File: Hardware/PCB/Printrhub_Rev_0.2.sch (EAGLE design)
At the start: 67 parts, among them J1 DM3D-SF, SW1 SPST_TACT-KMR2, SW2 SPST_TACT-KMR2, U1 MK20DX256VLH7, U2 AP1117E, U3 MAX308-SOT23, Y2 16Mhz/8pF

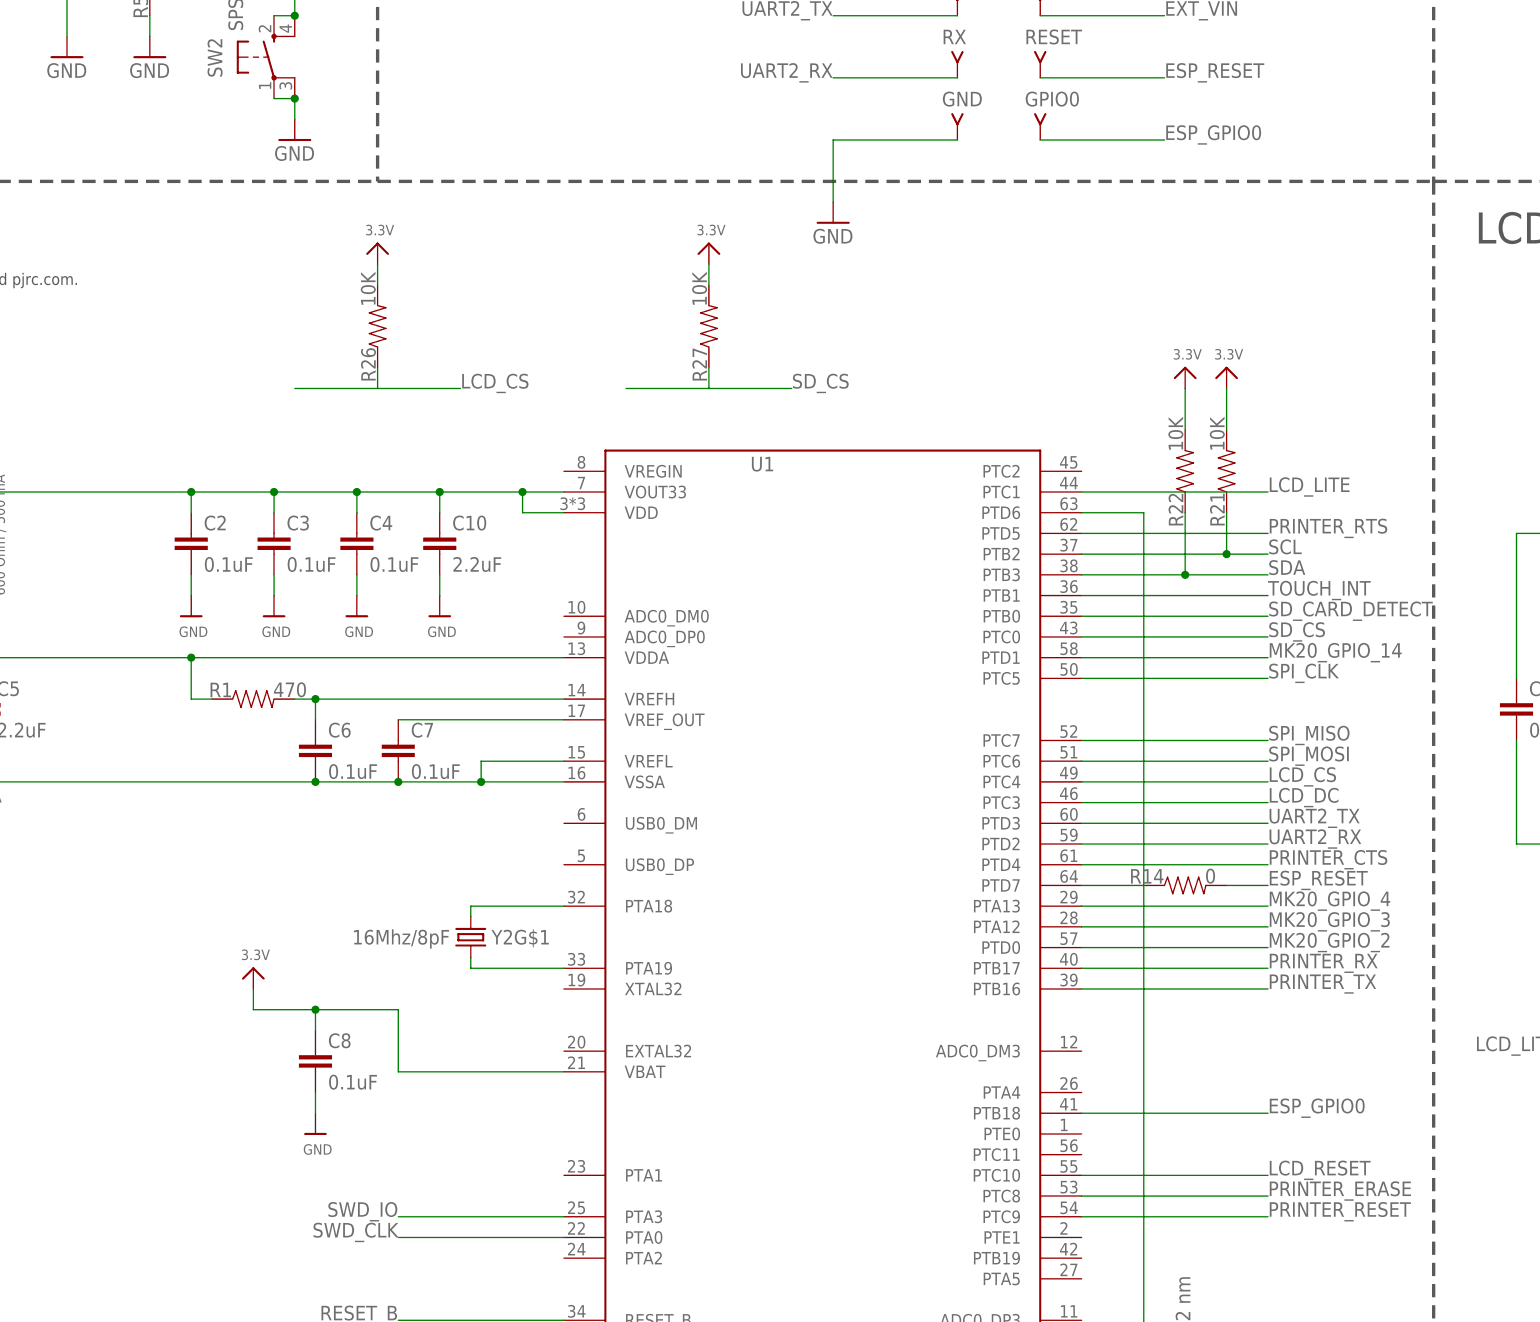
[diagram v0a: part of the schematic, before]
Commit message: Fixed a small bug in Rev 0.2 of the Printrhub PCB
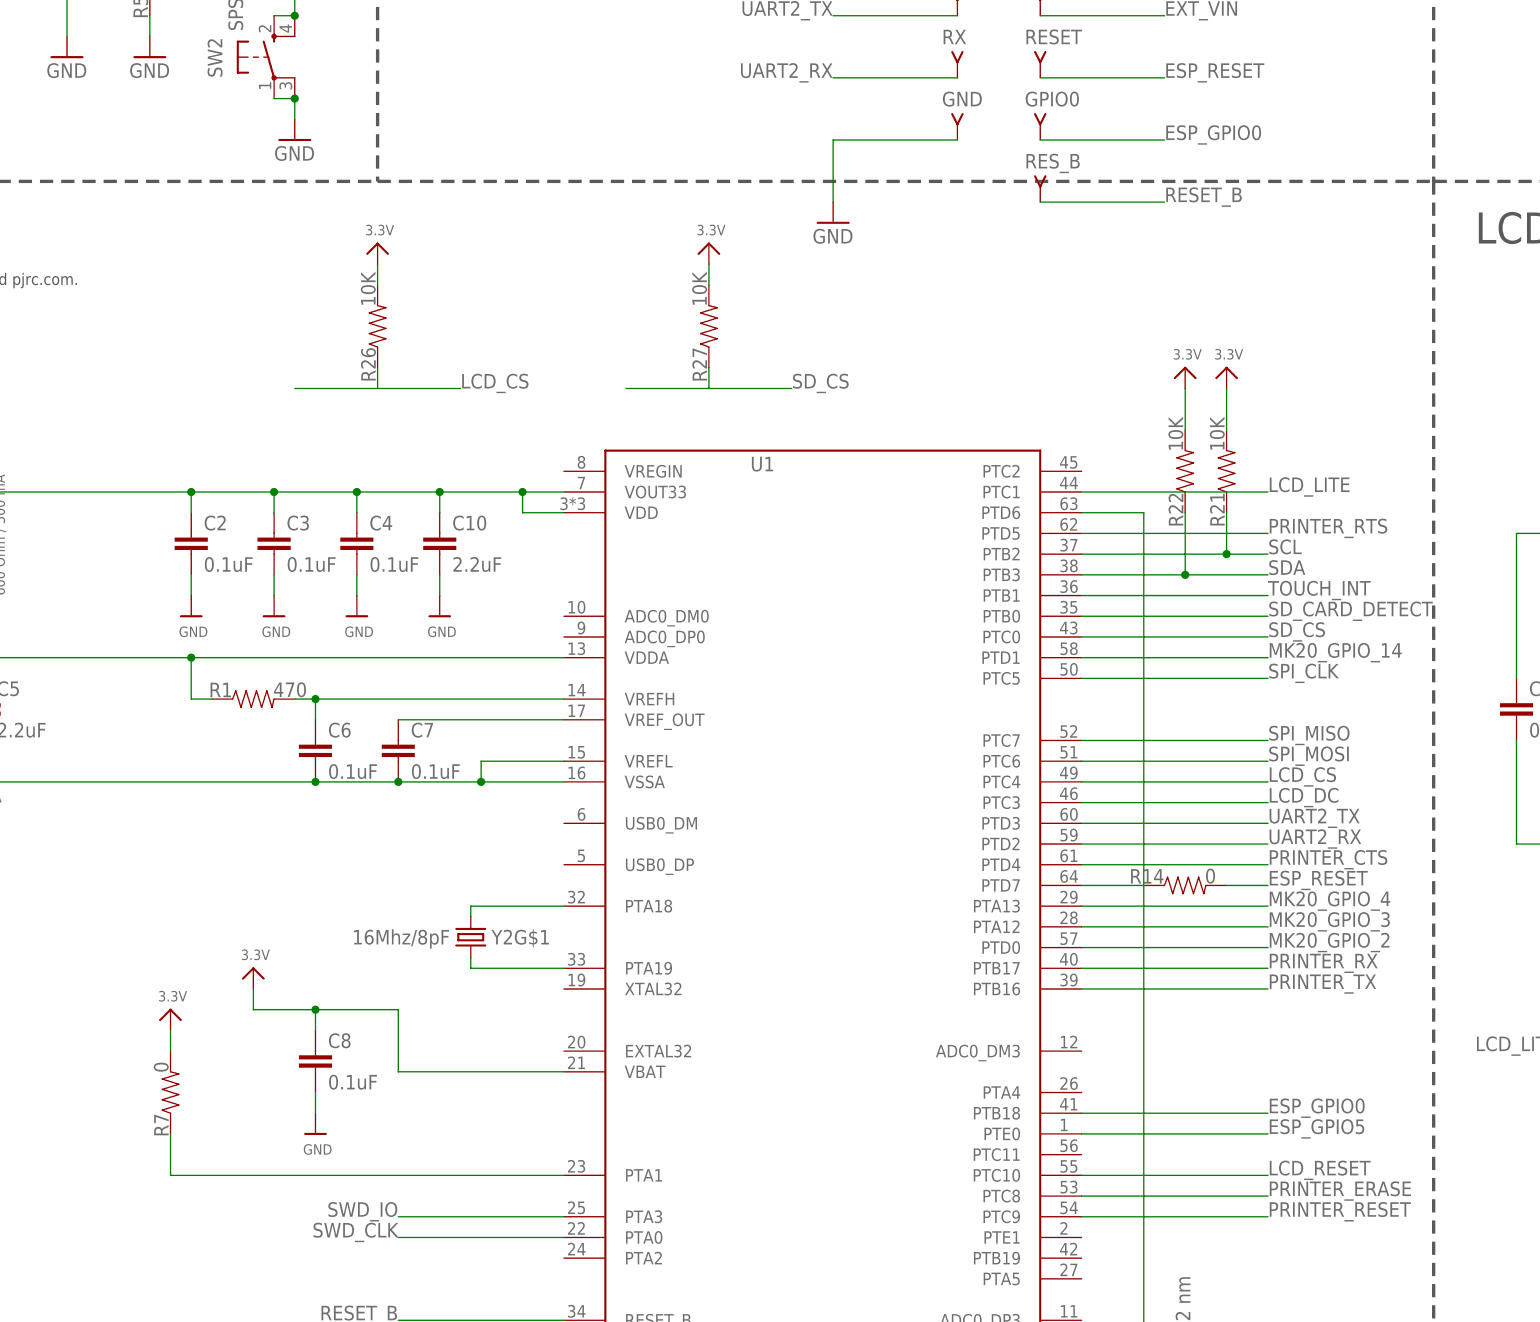
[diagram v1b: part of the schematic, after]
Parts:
- added R7: 0, appfruits:RESISTOR-0
- added RES_B: TPV-SMD-18RN, appfruits:TPV-SMD-18RN
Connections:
- new net N$3: R7.1, U1.PTA1
- net 3.3V: now also R7.2
- net ESP_GPIO5: now also U1.PTE0
- net RESET_B: now also RES_B.TP
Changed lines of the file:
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@@
 <part name="C9" library="appfruits" deviceset="CAPACITOR" device="-2.2UF" value="2.2uF"/>
 <part name="GND4" library="supply1" deviceset="GND" device=""/>
+<part name="RES_B" library="appfruits" deviceset="TPV" device="-SMD-18RN"/>
+<part name="U$7" library="microbuilder" deviceset="3.3V" device=""/>
+<part name="R7" library="appfruits" deviceset="RESISTOR" device="-0" value="0"/>
 </parts>
 <sheets>
@@
 <instance part="C9" gate="G$1" x="-60.96" y="17.78"/>
 <instance part="GND4" gate="1" x="-60.96" y="10.16"/>
+<instance part="RES_B" gate="G$1" x="198.12" y="-15.24"/>
+<instance part="U$7" gate="G$1" x="91.44" y="-116.84"/>
+<instance part="R7" gate="G$1" x="91.44" y="-127" rot="R90"/>
 </instances>
 <busses>
@@
 <pinref part="U$1" gate="G$1" pin="3.3V"/>
 </segment>
+<segment>
+<pinref part="R7" gate="G$1" pin="2"/>
+<pinref part="U$7" gate="G$1" pin="3.3V"/>
+<wire x1="91.44" y1="-121.92" x2="91.44" y2="-119.38" width="0.1524" layer="91"/>
+</segment>
 </net>
 <net name="SDA" class="0">
@@
 <wire x1="40.64" y1="17.78" x2="35.56" y2="17.78" width="0.1524" layer="91"/>
 <label x="35.56" y="17.78" size="1.778" layer="95" rot="MR0"/>
+</segment>
+<segment>
+<pinref part="RES_B" gate="G$1" pin="TP"/>
+<wire x1="198.12" y1="-17.78" x2="213.36" y2="-17.78" width="0.1524" layer="91"/>
+<label x="213.36" y="-17.78" size="1.778" layer="95"/>
 </segment>
 </net>
@@
 <wire x1="76.2" y1="25.4" x2="81.28" y2="25.4" width="0.1524" layer="91"/>
 <label x="81.28" y="25.4" size="1.778" layer="95"/>
+</segment>
+<segment>
+<pinref part="U1" gate="G$1" pin="PTE0"/>
+<wire x1="203.2" y1="-132.08" x2="226.06" y2="-132.08" width="0.1524" layer="91"/>
+<label x="226.06" y="-132.08" size="1.778" layer="95"/>
 </segment>
 </net>
@@
 </segment>
 </net>
+<net name="N$3" class="0">
+<segment>
+<pinref part="U1" gate="G$1" pin="PTA1"/>
+<pinref part="R7" gate="G$1" pin="1"/>
+<wire x1="139.7" y1="-137.16" x2="91.44" y2="-137.16" width="0.1524" layer="91"/>
+<wire x1="91.44" y1="-137.16" x2="91.44" y2="-132.08" width="0.1524" layer="91"/>
+</segment>
+</net>
